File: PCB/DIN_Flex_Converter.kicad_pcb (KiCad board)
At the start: 2 copper layers, 88.5 x 70 mm, 33 parts, among them IC1 ZXTR2005Z-13, J1 Screw_Terminal_01x04, J2 Screw_Terminal_01x04, J3 Conn_01x04_Socket, J4 Conn_02x06_Top_Bottom, J5 Conn_02x06_Top_Bottom, U1 74HC04

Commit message: Layout & Route Draft Complete
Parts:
- added C11: 0.1uF, Capacitor_SMD:C_1206_3216Metric, F.Cu at (167.4, 75.1)
- added C12: 10uF, Capacitor_SMD:C_1210_3225Metric, F.Cu at (134.2, 74.8)
- added C13: 0.1uF, Capacitor_SMD:C_1206_3216Metric, F.Cu at (138.0, 81.3)
- J4, J5: footprint Connector_PinSocket_2.54mm:PinSocket_2x06_P2.54mm_Vertical_SMD -> PSA:SSM-106-XXX-DV
- U1: footprint Package_SO:SOIC-14-16_3.9x9.9mm_P1.27mm -> PSA:SOIC127P600X175-14N
- moved C9 6.77 mm to (178.8, 89.2), turned to 0 degrees
- moved U1 2.81 mm to (161.1, 79.3)
- moved R1 2.30 mm to (135.4, 79.3)
- moved R3 2.26 mm to (133.0, 79.3)
- moved C7 1.80 mm to (154.4, 83.4)
- moved R2 1.80 mm to (154.3, 80.7)
- moved R4 1.80 mm to (154.3, 75.2)
- moved R5 1.80 mm to (154.3, 78.0)
- moved IC1 1.40 mm to (140.0, 76.4), turned to 180 degrees
- moved F1 0.60 mm to (127.8, 90.3)
- turned J4 to 90 degrees
- turned J5 to 90 degrees
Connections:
- J1 pad 1: GND -> /PWR_IN
- J1 pad 2: GND -> /PWR_IN
- J1 pad 3: /PWR_IN -> GND
- J1 pad 4: /PWR_IN -> GND
- J2 pad 1: GND -> /PWR OUT
- J2 pad 2: GND -> /PWR OUT
- J2 pad 3: /PWR OUT -> GND
- J2 pad 4: /PWR OUT -> GND
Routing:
- net /~{PWR_GOOD}: track 0.00 -> 83.2 mm, vias 0 -> 1
- net /~{PWR ENABLE}: track 0.00 -> 68.7 mm, vias 0 -> 1
- net /Trim: track 0.00 -> 65.4 mm, vias 0 -> 2
- net +5V: track 0.00 -> 57.3 mm
- net Net-(PS1-CURRENT_MONITOR): track 0.00 -> 39.3 mm, vias 0 -> 2
- net Net-(R3-Pad2): track 0.00 -> 36.7 mm
- net Net-(R1-Pad2): track 0.00 -> 34.0 mm
- net Net-(D1-A): track 0.00 -> 28.5 mm
- net /PWR_IN_PROT: track 0.00 -> 19.5 mm
- net Net-(D2-A): track 0.00 -> 19.3 mm
- net Net-(S1-NO): track 0.00 -> 15.5 mm
- net /I_MON: track 0.00 -> 14.0 mm
- net Net-(S1-NC): track 0.00 -> 13.7 mm
- net GND: track 0.00 -> 6.35 mm, vias 0 -> 163
- net Net-(R4-Pad2): track 0.00 -> 3.95 mm
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
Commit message: PCB Finalized and manufacturing files generated
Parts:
- turned R5 to 180 degrees
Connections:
- U1 pad 11: unconnected-(U1-Pad11) -> GND
- U1 pad 13: unconnected-(U1-Pad13) -> GND
- U1 pad 9: unconnected-(U1-Pad9) -> GND
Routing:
- net +5V: track 57.3 -> 52.6 mm
- net Net-(R4-Pad2): track 3.95 -> 2.79 mm
- net GND: vias 163 -> 168
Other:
- board text added: "+"
- board text added: "-"
- board text added: "Fuse"
- board text added: "GND"
- board text added: "GRN = Operational RED = Fault"
- board text added: "High Range Adj"
- board text added: "I_MON"
- board text added: "Input: 9V - 53V Output: 9.6 ~ 48V @ 8A 300W Total Power"
- board text added: "Low Range Adj"
- board text added: "PWR GOOD"
- board text added: "Power IN"
- board text added: "Power OUT"
- board text added: "Precision Sustainable Agriculture Mark Funderburk - 5/8/2024 DIN Mount DC-DC Flex Converter"
- board text added: "Range Select <-->"
- board text added: "~{EN}"
- board text added: "~{EN} Can be left floating"

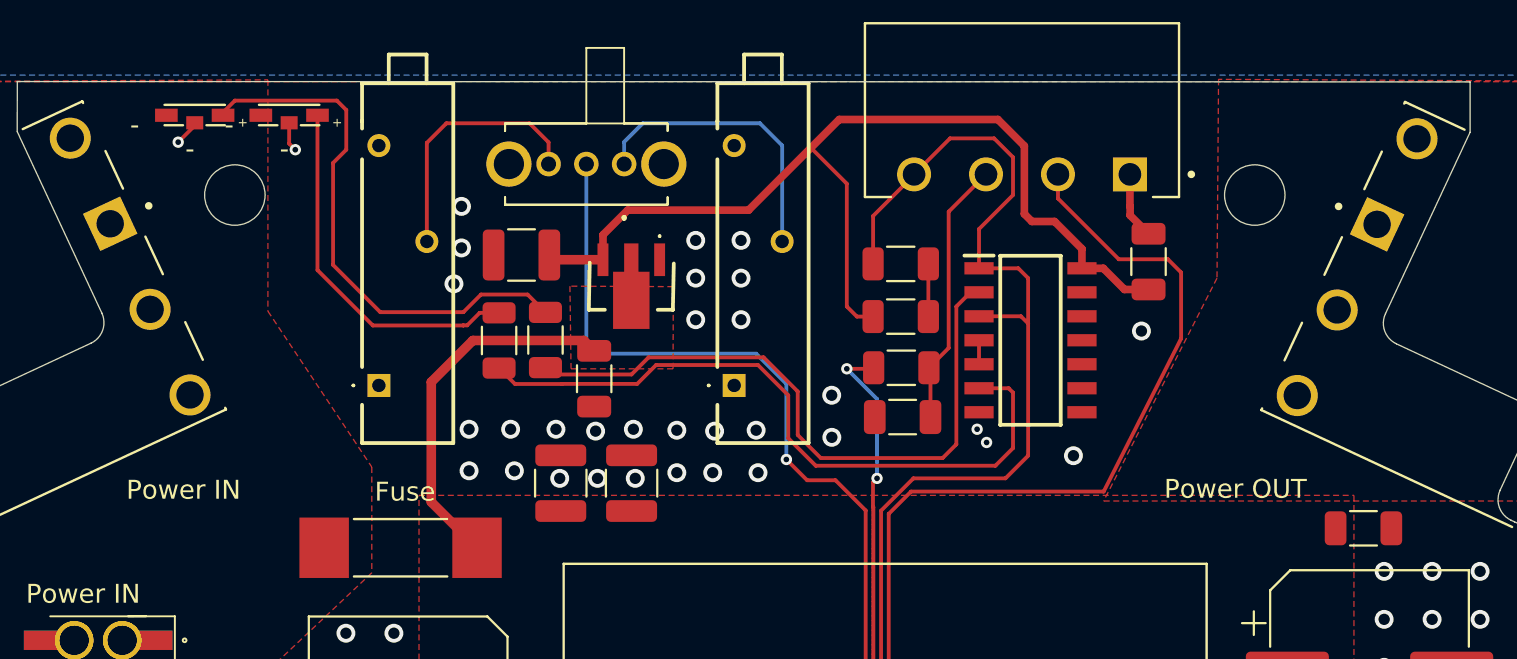
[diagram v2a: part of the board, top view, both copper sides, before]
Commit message: fixed LED footprint/routing and added enable jumper
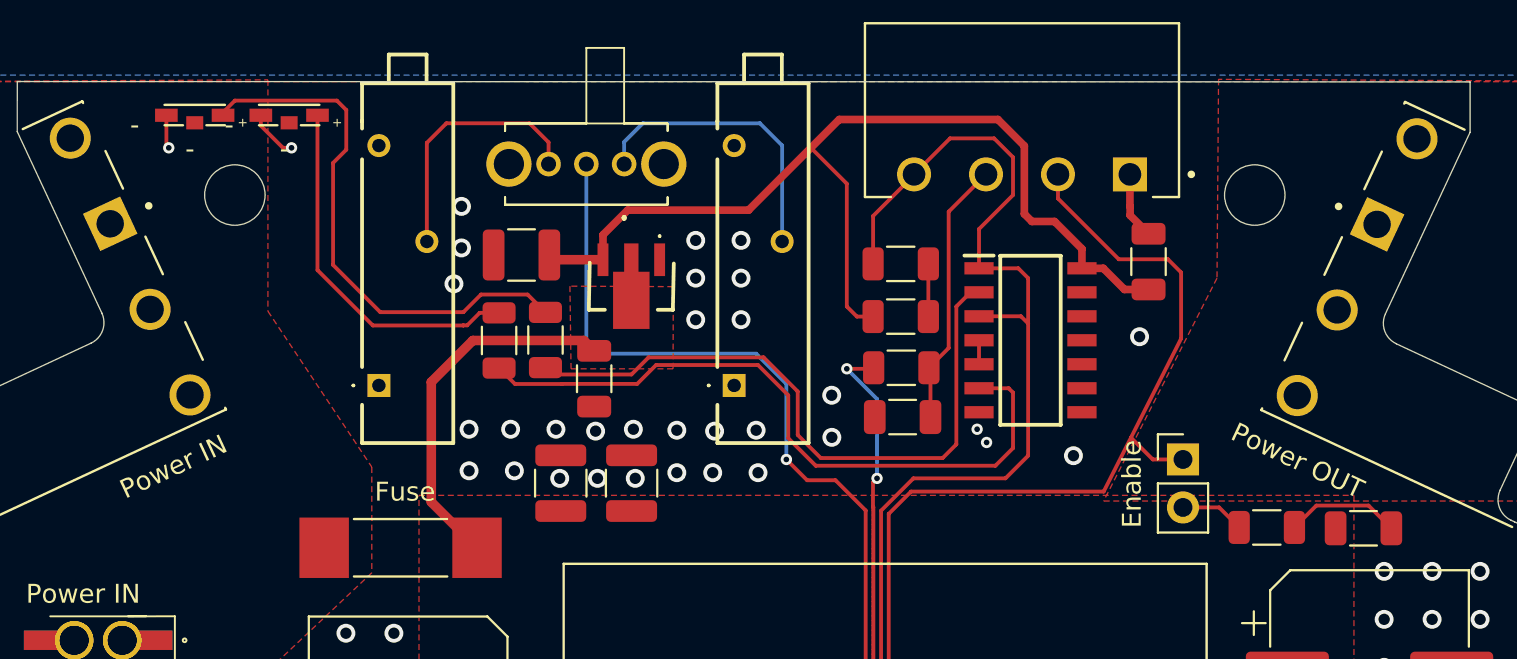
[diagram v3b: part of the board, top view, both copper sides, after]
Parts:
- added Enable: Conn_01x02_Pin, Connector_PinHeader_2.54mm:PinHeader_1x02_P2.54mm_Vertical, F.Cu at (169.2, 85.6)
- added R6: 1k, Resistor_SMD:R_1206_3216Metric, F.Cu at (173.6, 89.2)
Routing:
- net GND: track 6.35 -> 14.1 mm
- net Net-(J6-Pin_2): track 0.00 -> 3.41 mm
- net /~{PWR ENABLE}: track 68.7 -> 72.0 mm
